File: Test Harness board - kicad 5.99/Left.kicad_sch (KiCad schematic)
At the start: 27 parts

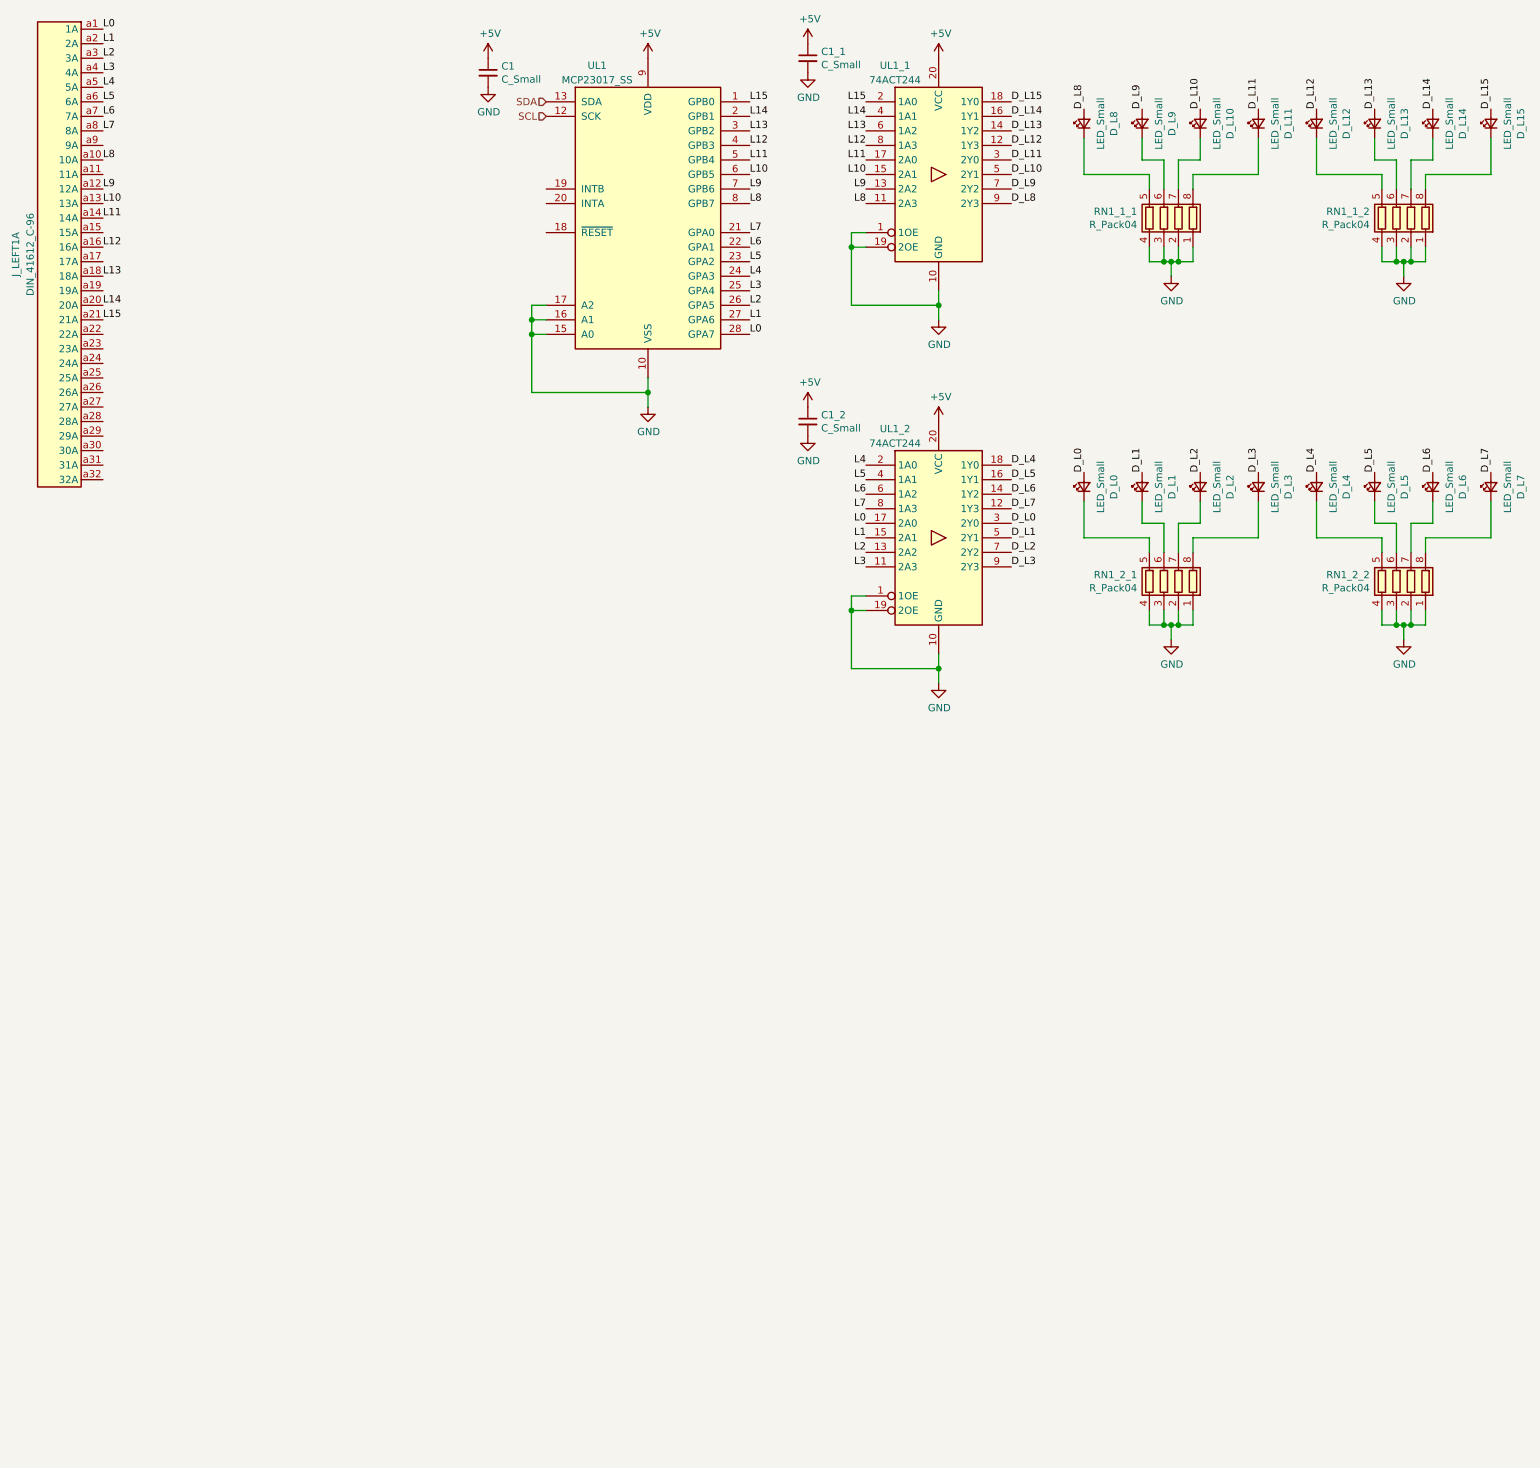
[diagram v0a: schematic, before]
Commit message: add the components to display the MAR bits
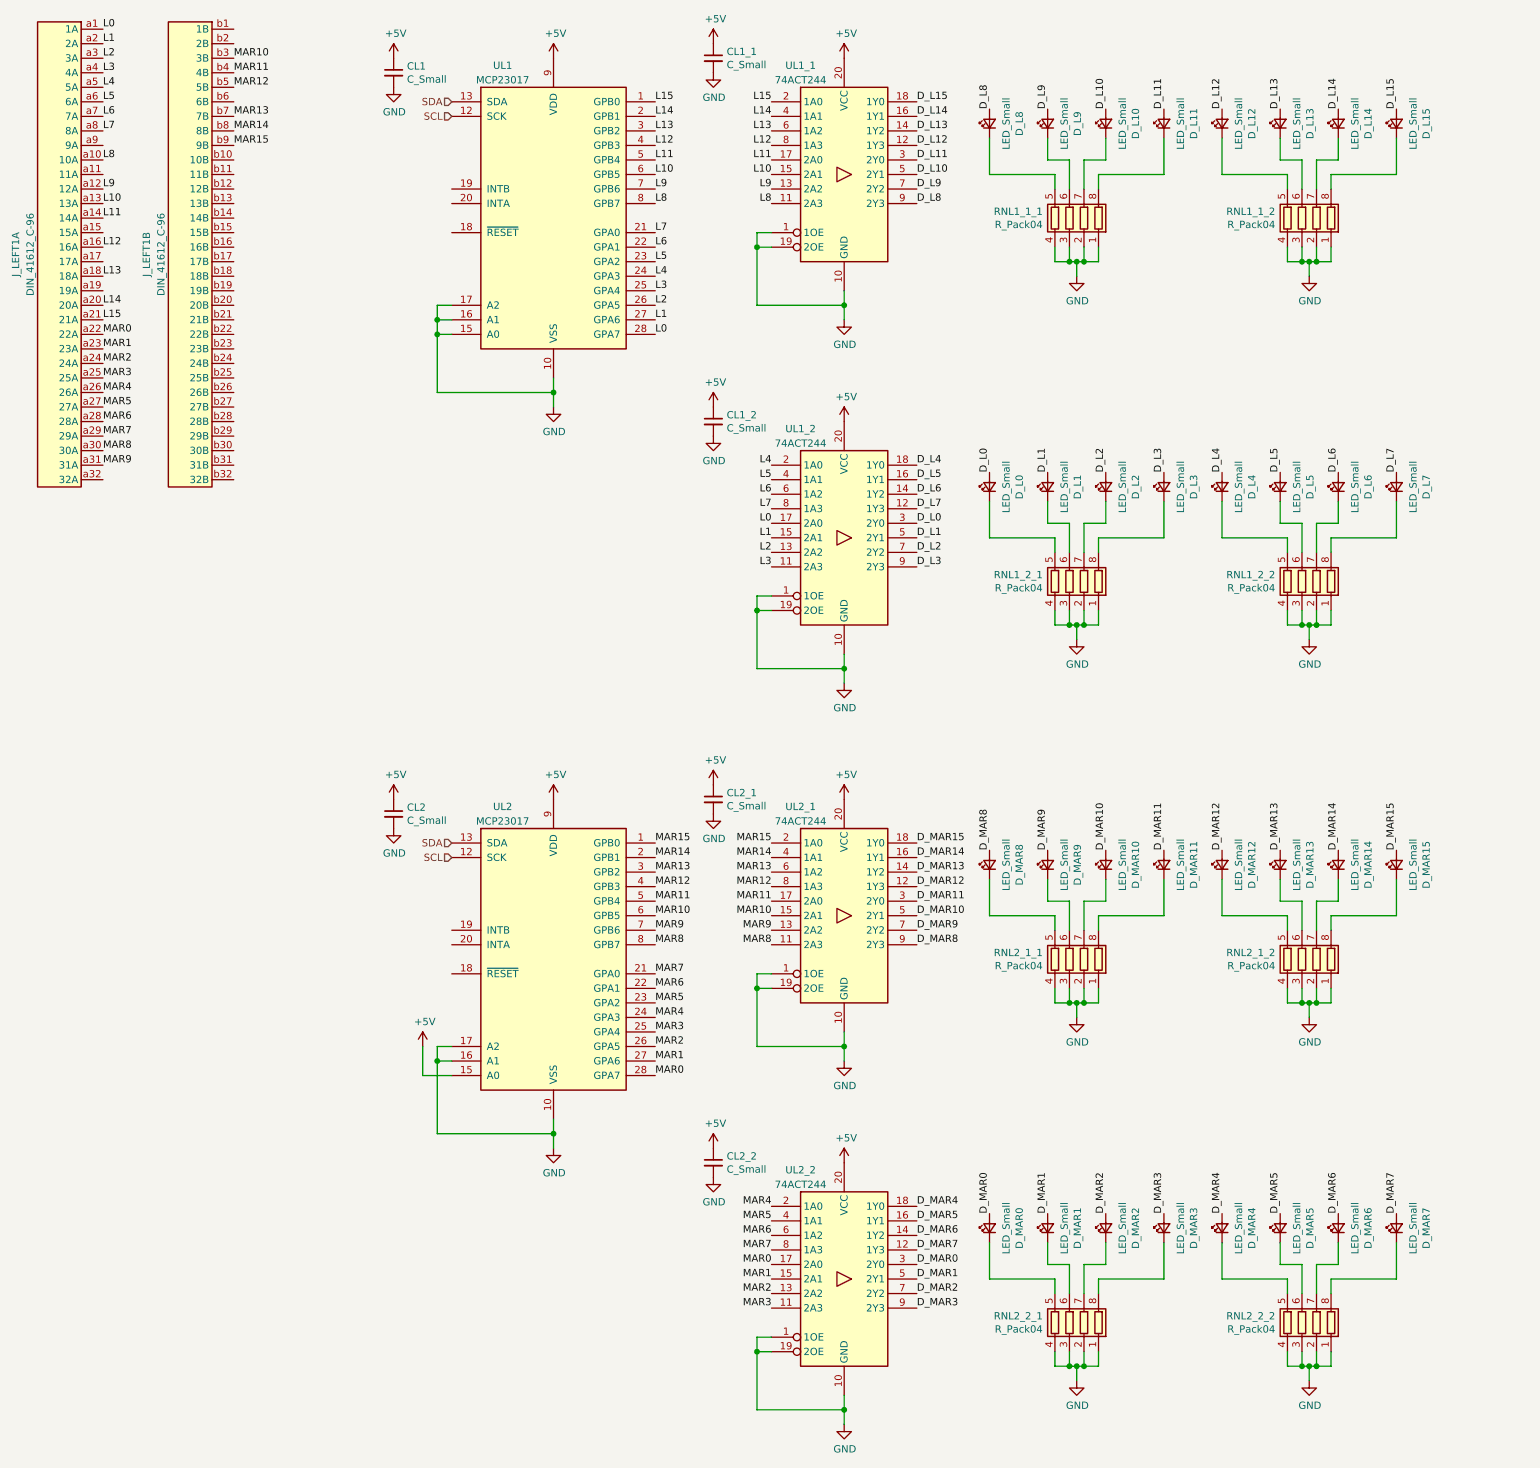
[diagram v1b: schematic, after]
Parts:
- added CL2, CL2_1, CL2_2: C_Small, Capacitor_SMD:C_1206_3216Metric, symbol Device:C_Small
- added D_MAR0, D_MAR1, D_MAR10, D_MAR11, D_MAR12, D_MAR13, D_MAR14, D_MAR15, D_MAR2, D_MAR3, D_MAR4, D_MAR5, D_MAR6, D_MAR7, D_MAR8, D_MAR9: LED_Small, LED_SMD:LED_1206_3216Metric_Castellated, symbol Device:LED_Small
- added unit 2 of J_LEFT1
- added RNL2_1_1, RNL2_1_2, RNL2_2_1, RNL2_2_2: R_Pack04, Resistor_SMD:R_Array_Convex_4x1206, symbol Device:R_Pack04
- added UL2: MCP23017, Package_SO:SSOP-28_5.3x10.2mm_P0.65mm, symbol Interface_Expansion:MCP23017_SS
- added UL2_1, UL2_2: 74ACT244, Package_SO:TSSOP-20_4.4x6.5mm_P0.65mm, symbol 74xx:74HCT244
- UL1: value MCP23017_SS -> MCP23017
- renumbered C1 to CL1, C1_1 to CL1_1, C1_2 to CL1_2, RN1_1_1 to RNL1_1_1, RN1_1_2 to RNL1_1_2, RN1_2_1 to RNL1_2_1, RN1_2_2 to RNL1_2_2
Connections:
- net +5V: now also CL2.1, CL2_1.1, CL2_2.1, UL2.15 (A0), UL2.9 (VDD), UL2_1.20 (VCC), UL2_2.20 (VCC)
- net GND: now also CL2.2, CL2_1.2, CL2_2.2, RNL2_1_1.1 (R1.1), RNL2_1_1.2 (R2.1), RNL2_1_1.3 (R3.1), RNL2_1_1.4 (R4.1), RNL2_1_2.1 (R1.1), RNL2_1_2.2 (R2.1), RNL2_1_2.3 (R3.1), RNL2_1_2.4 (R4.1), RNL2_2_1.1 (R1.1), RNL2_2_1.2 (R2.1), RNL2_2_1.3 (R3.1), RNL2_2_1.4 (R4.1), RNL2_2_2.1 (R1.1), RNL2_2_2.2 (R2.1), RNL2_2_2.3 (R3.1), RNL2_2_2.4 (R4.1), UL2.10 (VSS), UL2.16 (A1), UL2.17 (A2), UL2_1.1 (1OE), UL2_1.10 (GND), UL2_1.19 (2OE), UL2_2.1 (1OE), UL2_2.10 (GND), UL2_2.19 (2OE)
- net SCL: now also UL2.12 (SCK)
- net SDA: now also UL2.13 (SDA)
- net MAR0: now reaches J_LEFT1.a22 (22A)
- net MAR0: now also UL2.28 (GPA7), UL2_2.17 (2A0)
- net MAR1: now reaches J_LEFT1.a23 (23A)
- net MAR1: now also UL2.27 (GPA6), UL2_2.15 (2A1)
- net MAR2: now reaches J_LEFT1.a24 (24A)
- net MAR2: now also UL2.26 (GPA5), UL2_2.13 (2A2)
- net MAR3: now reaches J_LEFT1.a25 (25A)
- net MAR3: now also UL2.25 (GPA4), UL2_2.11 (2A3)
- net MAR4: now reaches J_LEFT1.a26 (26A)
- net MAR4: now also UL2.24 (GPA3), UL2_2.2 (1A0)
- net MAR5: now reaches J_LEFT1.a27 (27A)
- net MAR5: now also UL2.23 (GPA2), UL2_2.4 (1A1)
- net MAR6: now reaches J_LEFT1.a28 (28A)
- net MAR6: now also UL2.22 (GPA1), UL2_2.6 (1A2)
- net MAR7: now reaches J_LEFT1.a29 (29A)
- net MAR7: now also UL2.21 (GPA0), UL2_2.8 (1A3)
- net MAR8: now reaches J_LEFT1.a30 (30A)
- net MAR8: now also UL2.8 (GPB7), UL2_1.11 (2A3)
- net MAR9: now reaches J_LEFT1.a31 (31A)
- net MAR9: now also UL2.7 (GPB6), UL2_1.13 (2A2)
- new net: D_MAR0.1 (K), RNL2_2_1.5 (R4.2)
- new net: D_MAR1.1 (K), RNL2_2_1.6 (R3.2)
- new net: D_MAR15.1 (K), RNL2_1_2.8 (R1.2)
- new net: D_MAR10.1 (K), RNL2_1_1.7 (R2.2)
- new net: D_MAR9.1 (K), RNL2_1_1.6 (R3.2)
- new net: D_MAR11.1 (K), RNL2_1_1.8 (R1.2)
- new net: D_MAR2.1 (K), RNL2_2_1.7 (R2.2)
- new net: D_MAR14.1 (K), RNL2_1_2.7 (R2.2)
- new net: D_MAR8.1 (K), RNL2_1_1.5 (R4.2)
- new net: D_MAR6.1 (K), RNL2_2_2.7 (R2.2)
- new net: D_MAR4.1 (K), RNL2_2_2.5 (R4.2)
- new net: D_MAR3.1 (K), RNL2_2_1.8 (R1.2)
- new net: D_MAR7.1 (K), RNL2_2_2.8 (R1.2)
- new net: D_MAR12.1 (K), RNL2_1_2.5 (R4.2)
- new net: D_MAR13.1 (K), RNL2_1_2.6 (R3.2)
- new net: D_MAR5.1 (K), RNL2_2_2.6 (R3.2)
- new net D_MAR0: D_MAR0.2 (A), UL2_2.3 (2Y0)
- new net D_MAR1: D_MAR1.2 (A), UL2_2.5 (2Y1)
- new net D_MAR10: D_MAR10.2 (A), UL2_1.5 (2Y1)
- new net D_MAR11: D_MAR11.2 (A), UL2_1.3 (2Y0)
- new net D_MAR12: D_MAR12.2 (A), UL2_1.12 (1Y3)
- new net D_MAR13: D_MAR13.2 (A), UL2_1.14 (1Y2)
- new net D_MAR14: D_MAR14.2 (A), UL2_1.16 (1Y1)
- new net D_MAR15: D_MAR15.2 (A), UL2_1.18 (1Y0)
- new net D_MAR2: D_MAR2.2 (A), UL2_2.7 (2Y2)
- new net D_MAR3: D_MAR3.2 (A), UL2_2.9 (2Y3)
- new net D_MAR4: D_MAR4.2 (A), UL2_2.18 (1Y0)
- new net D_MAR5: D_MAR5.2 (A), UL2_2.16 (1Y1)
- new net D_MAR6: D_MAR6.2 (A), UL2_2.14 (1Y2)
- new net D_MAR7: D_MAR7.2 (A), UL2_2.12 (1Y3)
- new net D_MAR8: D_MAR8.2 (A), UL2_1.9 (2Y3)
- new net D_MAR9: D_MAR9.2 (A), UL2_1.7 (2Y2)
- new net MAR10: J_LEFT1.b3 (3B), UL2.6 (GPB5), UL2_1.15 (2A1)
- new net MAR11: J_LEFT1.b4 (4B), UL2.5 (GPB4), UL2_1.17 (2A0)
- new net MAR12: J_LEFT1.b5 (5B), UL2.4 (GPB3), UL2_1.8 (1A3)
- new net MAR13: J_LEFT1.b7 (7B), UL2.3 (GPB2), UL2_1.6 (1A2)
- new net MAR14: J_LEFT1.b8 (8B), UL2.2 (GPB1), UL2_1.4 (1A1)
- new net MAR15: J_LEFT1.b9 (9B), UL2.1 (GPB0), UL2_1.2 (1A0)
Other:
- moved on the sheet: CL1, CL1_1, CL1_2, D_L0, D_L1, D_L10, D_L11, D_L12, D_L13, D_L14, D_L15, D_L2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

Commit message: restart on the test harness, made a more compact design (will need the 4 layers though)
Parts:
- added CL3, CL3_1, CL3_2, CL4, CL4_1, CL4_2, CL5, CL5_1, CL5_2: C_Small, Capacitor_SMD:C_1206_3216Metric, symbol Device:C_Small
- added D_A0, D_A1, D_A10, D_A11, D_A12, D_A13, D_A14, D_A15, D_A16, D_A17, D_A18, D_A19, D_A2, D_A20, D_A21, D_A3, D_A4, D_A5, D_A6, D_A7, D_A8, D_A9, D_D0, D_D1, D_D2, D_D3, D_D4, D_D5, D_D6, D_D7, D_IR2, D_IR3, D_MEMORY1, D_MEMREF1, D_XL_MDR_HI1, D_XL_MDR_LO1, D__IR1, D__IRQ4, D__PSEL1, D__RD1, D__RESET1, D__STOP_CLK1, D__WR1: LED_Small, LED_SMD:LED_1206_3216Metric_Castellated, symbol Device:LED_Small
- added unit 3 of J_LEFT1
- added RNL3_1_1, RNL3_1_2, RNL3_2_1, RNL3_2_2, RNL4_1_1, RNL4_1_2, RNL4_2_1, RNL4_2_2, RNL5_1_1, RNL5_1_2, RNL5_2_1, RNL5_2_2: R_Pack04, Resistor_SMD:R_Array_Convex_4x1206, symbol Device:R_Pack04
- added UL3, UL4, UL5: MCP23017, Package_SO:SSOP-28_5.3x10.2mm_P0.65mm, symbol Interface_Expansion:MCP23017_SS
- added UL3_1, UL3_2, UL4_1, UL4_2, UL5_1, UL5_2: 74ACT244, Package_SO:TSSOP-20_4.4x6.5mm_P0.65mm, symbol 74xx:74HCT244
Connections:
- net +5V: now also CL3.1, CL3_1.1, CL3_2.1, CL4.1, CL4_1.1, CL4_2.1, CL5.1, CL5_1.1, CL5_2.1, UL3.16 (A1), UL3.9 (VDD), UL3_1.20 (VCC), UL3_2.20 (VCC), UL4.15 (A0), UL4.16 (A1), UL4.9 (VDD), UL4_1.20 (VCC), UL4_2.20 (VCC), UL5.15 (A0), UL5.9 (VDD), UL5_1.20 (VCC), UL5_2.20 (VCC)
- net GND: now also CL3.2, CL3_1.2, CL3_2.2, CL4.2, CL4_1.2, CL4_2.2, CL5.2, CL5_1.2, CL5_2.2, RNL3_1_1.1 (R1.1), RNL3_1_1.2 (R2.1), RNL3_1_1.3 (R3.1), RNL3_1_1.4 (R4.1), RNL3_1_2.1 (R1.1), RNL3_1_2.2 (R2.1), RNL3_1_2.3 (R3.1), RNL3_1_2.4 (R4.1), RNL3_2_1.1 (R1.1), RNL3_2_1.2 (R2.1), RNL3_2_1.3 (R3.1), RNL3_2_1.4 (R4.1), RNL3_2_2.1 (R1.1), RNL3_2_2.2 (R2.1), RNL3_2_2.3 (R3.1), RNL3_2_2.4 (R4.1), RNL4_1_1.1 (R1.1), RNL4_1_1.2 (R2.1), RNL4_1_1.3 (R3.1), RNL4_1_1.4 (R4.1), RNL4_1_2.1 (R1.1), RNL4_1_2.2 (R2.1), RNL4_1_2.3 (R3.1), RNL4_1_2.4 (R4.1), RNL4_2_1.1 (R1.1), RNL4_2_1.2 (R2.1), RNL4_2_1.3 (R3.1), RNL4_2_1.4 (R4.1), RNL4_2_2.1 (R1.1), RNL4_2_2.2 (R2.1), RNL4_2_2.3 (R3.1), RNL4_2_2.4 (R4.1), RNL5_1_1.1 (R1.1), RNL5_1_1.2 (R2.1), RNL5_1_1.3 (R3.1), RNL5_1_1.4 (R4.1), RNL5_1_2.1 (R1.1), RNL5_1_2.2 (R2.1), RNL5_1_2.3 (R3.1), RNL5_1_2.4 (R4.1), RNL5_2_1.1 (R1.1), RNL5_2_1.2 (R2.1), RNL5_2_1.3 (R3.1), RNL5_2_1.4 (R4.1), RNL5_2_2.1 (R1.1), RNL5_2_2.2 (R2.1), RNL5_2_2.3 (R3.1), RNL5_2_2.4 (R4.1), UL3.10 (VSS), UL3.15 (A0), UL3.17 (A2), UL3_1.1 (1OE), UL3_1.10 (GND), UL3_1.19 (2OE), UL3_2.1 (1OE), UL3_2.10 (GND), UL3_2.19 (2OE), UL4.10 (VSS), UL4.17 (A2), UL4_1.1 (1OE), UL4_1.10 (GND), UL4_1.11 (2A3), UL4_1.13 (2A2), UL4_1.19 (2OE), UL4_2.1 (1OE), UL4_2.10 (GND), UL4_2.19 (2OE), UL5.10 (VSS), UL5.16 (A1), UL5.17 (A2), UL5_1.1 (1OE), UL5_1.10 (GND), UL5_1.19 (2OE), UL5_2.1 (1OE), UL5_2.10 (GND), UL5_2.19 (2OE)
- net SCL: now also UL3.12 (SCK), UL4.12 (SCK), UL5.12 (SCK)
- net SDA: now also UL3.13 (SDA), UL4.13 (SDA), UL5.13 (SDA)
- net MEMREF: now reaches J_LEFT1.b10 (10B)
- net MEMREF: now also UL5.3 (GPB2), UL5_1.6 (1A2)
- net _RESET: now reaches J_LEFT1.b14 (14B)
- net _RESET: now also UL5.4 (GPB3), UL5_1.8 (1A3)
- net _STOP_CLK: now reaches J_LEFT1.b15 (15B)
- net _STOP_CLK: now also UL5.5 (GPB4), UL5_1.17 (2A0)
- net _WR: now reaches J_LEFT1.b16 (16B)
- net _WR: now also UL5.23 (GPA2), UL5_2.6 (1A2)
- net XL_MDR_HI: now reaches J_LEFT1.b18 (18B)
- net XL_MDR_HI: now also UL5.25 (GPA4), UL5_2.17 (2A0)
- net XL_MDR_LO: now reaches J_LEFT1.b19 (19B)
- net XL_MDR_LO: now also UL5.24 (GPA3), UL5_2.8 (1A3)
- net MEMORY: now reaches J_LEFT1.b2 (2B)
- net MEMORY: now also UL5.1 (GPB0), UL5_1.2 (1A0)
- net _RD: now reaches J_LEFT1.b25 (25B)
- net _RD: now also UL5.22 (GPA1), UL5_2.4 (1A1)
- net _IRQ4: now reaches J_LEFT1.b26 (26B)
- net _IRQ4: now also UL5.8 (GPB7), UL5_1.11 (2A3)
- net IR1: now reaches J_LEFT1.b28 (28B)
- net IR1: now also UL5.28 (GPA7), UL5_2.11 (2A3)
- net IR2: now reaches J_LEFT1.b29 (29B)
- net IR2: now also UL5.27 (GPA6), UL5_2.13 (2A2)
- net IR3: now reaches J_LEFT1.b30 (30B)
- net IR3: now also UL5.26 (GPA5), UL5_2.15 (2A1)
- net _PSEL1: now reaches J_LEFT1.b6 (6B)
- net _PSEL1: now also UL5.21 (GPA0), UL5_2.2 (1A0)
- new net: D__RD1.1 (K), RNL5_2_1.7 (R2.2)
- new net: D_A16.1 (K), RNL3_1_1.7 (R2.2)
- new net: D_D6.1 (K), RNL4_2_2.7 (R2.2)
- new net: D_A14.1 (K), RNL3_1_1.5 (R4.2)
- new net: D_A6.1 (K), RNL3_2_1.5 (R4.2)
- new net: D_A7.1 (K), RNL3_2_1.6 (R3.2)
- new net: D_A8.1 (K), RNL3_2_1.7 (R2.2)
- new net: D_A9.1 (K), RNL3_2_1.8 (R1.2)
- new net: D_A15.1 (K), RNL3_1_1.6 (R3.2)
- new net: D_A17.1 (K), RNL3_1_1.8 (R1.2)
- new net: D_A0.1 (K), RNL4_1_1.7 (R2.2)
- new net: D_XL_MDR_LO1.1 (K), RNL5_2_1.5 (R4.2)
- new net: D_A20.1 (K), RNL3_1_2.7 (R2.2)
- new net: D__WR1.1 (K), RNL5_2_1.6 (R3.2)
- new net: D__PSEL1.1 (K), RNL5_2_1.8 (R1.2)
- new net: D__IR1.1 (K), RNL5_2_2.5 (R4.2)
- new net: D_IR2.1 (K), RNL5_2_2.6 (R3.2)
- new net: D_IR3.1 (K), RNL5_2_2.7 (R2.2)
- new net: D_XL_MDR_HI1.1 (K), RNL5_2_2.8 (R1.2)
- new net: D_D3.1 (K), RNL4_2_1.8 (R1.2)
- new net: D_A11.1 (K), RNL3_2_2.6 (R3.2)
- new net: D_A1.1 (K), RNL4_1_1.8 (R1.2)
- new net: D_A19.1 (K), RNL3_1_2.6 (R3.2)
- new net: D_MEMREF1.1 (K), RNL5_1_1.5 (R4.2)
- new net: D_MEMORY1.1 (K), RNL5_1_1.6 (R3.2)
- new net: D__RESET1.1 (K), RNL5_1_1.7 (R2.2)
- new net: D__STOP_CLK1.1 (K), RNL5_1_1.8 (R1.2)
- new net: D_D7.1 (K), RNL4_2_2.8 (R1.2)
- new net: D_D1.1 (K), RNL4_2_1.6 (R3.2)
- new net: D__IRQ4.1 (K), RNL5_1_2.7 (R2.2)
- new net: D_A5.1 (K), RNL4_1_2.8 (R1.2)
- new net: D_D5.1 (K), RNL4_2_2.6 (R3.2)
- new net: D_D4.1 (K), RNL4_2_2.5 (R4.2)
- new net: D_A21.1 (K), RNL3_1_2.8 (R1.2)
- new net: D_D2.1 (K), RNL4_2_1.7 (R2.2)
- new net: D_D0.1 (K), RNL4_2_1.5 (R4.2)
- new net: D_A4.1 (K), RNL4_1_2.7 (R2.2)
- new net: D_A12.1 (K), RNL3_2_2.7 (R2.2)
- new net: D_A2.1 (K), RNL4_1_2.5 (R4.2)
- new net: D_A3.1 (K), RNL4_1_2.6 (R3.2)
- new net: D_A10.1 (K), RNL3_2_2.5 (R4.2)
- new net: D_A18.1 (K), RNL3_1_2.5 (R4.2)
- new net: D_A13.1 (K), RNL3_2_2.8 (R1.2)
- new net A0: J_LEFT1.c1 (1C), UL4.6 (GPB5), UL4_1.15 (2A1)
- new net A1: J_LEFT1.c2 (2C), UL4.5 (GPB4), UL4_1.17 (2A0)
- new net A10: J_LEFT1.c12 (12C), UL3.24 (GPA3), UL3_2.8 (1A3)
- new net A11: J_LEFT1.c13 (13C), UL3.23 (GPA2), UL3_2.6 (1A2)
- new net A12: J_LEFT1.c14 (14C), UL3.22 (GPA1), UL3_2.4 (1A1)
- new net A13: J_LEFT1.c15 (15C), UL3.21 (GPA0), UL3_2.2 (1A0)
- new net A14: J_LEFT1.c16 (16C), UL3.8 (GPB7), UL3_1.11 (2A3)
- new net A15: J_LEFT1.c17 (17C), UL3.7 (GPB6), UL3_1.13 (2A2)
- new net A16: J_LEFT1.c18 (18C), UL3.6 (GPB5), UL3_1.15 (2A1)
- new net A17: J_LEFT1.c19 (19C), UL3.5 (GPB4), UL3_1.17 (2A0)
- new net A18: J_LEFT1.c20 (20C), UL3.4 (GPB3), UL3_1.8 (1A3)
- new net A19: J_LEFT1.c21 (21C), UL3.3 (GPB2), UL3_1.6 (1A2)
- new net A2: J_LEFT1.c3 (3C), UL4.4 (GPB3), UL4_1.8 (1A3)
- new net A20: J_LEFT1.c22 (22C), UL3.2 (GPB1), UL3_1.4 (1A1)
- new net A21: J_LEFT1.c23 (23C), UL3.1 (GPB0), UL3_1.2 (1A0)
- new net A3: J_LEFT1.c4 (4C), UL4.3 (GPB2), UL4_1.6 (1A2)
- new net A4: J_LEFT1.c5 (5C), UL4.2 (GPB1), UL4_1.4 (1A1)
- new net A5: J_LEFT1.c6 (6C), UL4.1 (GPB0), UL4_1.2 (1A0)
- new net A6: J_LEFT1.c7 (7C), UL3.28 (GPA7), UL3_2.11 (2A3)
- new net A7: J_LEFT1.c8 (8C), UL3.27 (GPA6), UL3_2.13 (2A2)
- new net A8: J_LEFT1.c10 (10C), UL3.26 (GPA5), UL3_2.15 (2A1)
- new net A9: J_LEFT1.c11 (11C), UL3.25 (GPA4), UL3_2.17 (2A0)
- new net D0: J_LEFT1.c24 (24C), UL4.28 (GPA7), UL4_2.17 (2A0)
- new net D1: J_LEFT1.c25 (25C), UL4.27 (GPA6), UL4_2.15 (2A1)
- new net D2: J_LEFT1.c26 (26C), UL4.26 (GPA5), UL4_2.13 (2A2)
- new net D3: J_LEFT1.c27 (27C), UL4.25 (GPA4), UL4_2.11 (2A3)
- new net D4: J_LEFT1.c28 (28C), UL4.24 (GPA3), UL4_2.2 (1A0)
- new net D5: J_LEFT1.c29 (29C), UL4.23 (GPA2), UL4_2.4 (1A1)
- new net D6: J_LEFT1.c30 (30C), UL4.22 (GPA1), UL4_2.6 (1A2)
- new net D7: J_LEFT1.c31 (31C), UL4.21 (GPA0), UL4_2.8 (1A3)
- new net D_A0: D_A0.2 (A), UL4_1.5 (2Y1)
- new net D_A1: D_A1.2 (A), UL4_1.3 (2Y0)
- new net D_A10: D_A10.2 (A), UL3_2.12 (1Y3)
- new net D_A11: D_A11.2 (A), UL3_2.14 (1Y2)
- new net D_A12: D_A12.2 (A), UL3_2.16 (1Y1)
- new net D_A13: D_A13.2 (A), UL3_2.18 (1Y0)
- new net D_A14: D_A14.2 (A), UL3_1.9 (2Y3)
- new net D_A15: D_A15.2 (A), UL3_1.7 (2Y2)
- new net D_A16: D_A16.2 (A), UL3_1.5 (2Y1)
- new net D_A17: D_A17.2 (A), UL3_1.3 (2Y0)
- new net D_A18: D_A18.2 (A), UL3_1.12 (1Y3)
- new net D_A19: D_A19.2 (A), UL3_1.14 (1Y2)
- new net D_A2: D_A2.2 (A), UL4_1.12 (1Y3)
- new net D_A20: D_A20.2 (A), UL3_1.16 (1Y1)
- new net D_A21: D_A21.2 (A), UL3_1.18 (1Y0)
- new net D_A3: D_A3.2 (A), UL4_1.14 (1Y2)
- new net D_A4: D_A4.2 (A), UL4_1.16 (1Y1)
- new net D_A5: D_A5.2 (A), UL4_1.18 (1Y0)
- new net D_A6: D_A6.2 (A), UL3_2.9 (2Y3)
- new net D_A7: D_A7.2 (A), UL3_2.7 (2Y2)
- new net D_A8: D_A8.2 (A), UL3_2.5 (2Y1)
- new net D_A9: D_A9.2 (A), UL3_2.3 (2Y0)
- new net D_D0: D_D0.2 (A), UL4_2.3 (2Y0)
- new net D_D1: D_D1.2 (A), UL4_2.5 (2Y1)
- new net D_D2: D_D2.2 (A), UL4_2.7 (2Y2)
- new net D_D3: D_D3.2 (A), UL4_2.9 (2Y3)
- new net D_D4: D_D4.2 (A), UL4_2.18 (1Y0)
- new net D_D5: D_D5.2 (A), UL4_2.16 (1Y1)
- new net D_D6: D_D6.2 (A), UL4_2.14 (1Y2)
- new net D_D7: D_D7.2 (A), UL4_2.12 (1Y3)
- new net D_IR1: D__IR1.2 (A), UL5_2.9 (2Y3)
- new net D_IR2: D_IR2.2 (A), UL5_2.7 (2Y2)
- new net D_IR3: D_IR3.2 (A), UL5_2.5 (2Y1)
- new net D_MEMORY: D_MEMORY1.2 (A), UL5_1.18 (1Y0)
- new net D_MEMREF: D_MEMREF1.2 (A), UL5_1.14 (1Y2)
- new net D_WR: UL5_2.14 (1Y2)
- new net D_XL_MDR_HI: D_XL_MDR_HI1.2 (A), UL5_2.3 (2Y0)
- new net D_XL_MDR_LO: D_XL_MDR_LO1.2 (A), UL5_2.12 (1Y3)
- new net D__IRQ4: D__IRQ4.2 (A), UL5_1.9 (2Y3)
- new net D__PSEL1: D__PSEL1.2 (A), UL5_2.18 (1Y0)
- new net D__RD: D__RD1.2 (A), UL5_2.16 (1Y1)
- new net D__RESET: D__RESET1.2 (A), UL5_1.12 (1Y3)
- new net D__STOP_CLK: D__STOP_CLK1.2 (A), UL5_1.3 (2Y0)
- new net D__WR: D__WR1.2 (A)
- no-connect marks 0 -> 4
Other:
- moved on the sheet: CL1, CL1_1, CL1_2, CL2, CL2_1, CL2_2, D_L0, D_L1, D_L10, D_L11, D_L12, D_L13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

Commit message: restart with the test harness board
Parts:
- J_LEFT1: footprint (none) -> Connector_DIN:DIN41612_C_3x32_Male_Horizontal_THT
- UL1, UL2, UL3, UL4, UL5: footprint Package_SO:SSOP-28_5.3x10.2mm_P0.65mm -> Package_SO:SOIC-28W_7.5x17.9mm_P1.27mm
- UL1_1, UL1_2, UL2_1, UL2_2, UL3_1, UL3_2, UL4_1, UL4_2, UL5_1, UL5_2: footprint Package_SO:TSSOP-20_4.4x6.5mm_P0.65mm -> Package_SO:SOIC-20W_7.5x12.8mm_P1.27mm
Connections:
- net D_WR is gone; now on net D__WR: UL5_2.14 (1Y2)
- net +5V: now also J_LEFT1.a32 (32A), J_LEFT1.b1 (1B), J_LEFT1.b11 (11B), J_LEFT1.b13 (13B), J_LEFT1.b17 (17B), J_LEFT1.b21 (21B), J_LEFT1.b24 (24B), J_LEFT1.b27 (27B), J_LEFT1.b32 (32B), J_LEFT1.c32 (32C)
- net A10: now also UL3.4 (GPB3); no longer UL3.24 (GPA3)
- net A11: now also UL3.3 (GPB2); no longer UL3.23 (GPA2)
- net A12: now also UL3.2 (GPB1); no longer UL3.22 (GPA1)
- net A13: now also UL3.1 (GPB0); no longer UL3.21 (GPA0)
- net A14: now also UL3.28 (GPA7); no longer UL3.8 (GPB7)
- net A15: now also UL3.27 (GPA6); no longer UL3.7 (GPB6)
- net A16: now also UL3.26 (GPA5); no longer UL3.6 (GPB5)
- net A17: now also UL3.25 (GPA4); no longer UL3.5 (GPB4)
- net A18: now also UL3.24 (GPA3); no longer UL3.4 (GPB3)
- net A19: now also UL3.23 (GPA2); no longer UL3.3 (GPB2)
- net A20: now also UL3.22 (GPA1); no longer UL3.2 (GPB1)
- net A21: now also UL3.21 (GPA0); no longer UL3.1 (GPB0)
- net A6: now also UL3.8 (GPB7); no longer UL3.28 (GPA7)
- net A7: now also UL3.7 (GPB6); no longer UL3.27 (GPA6)
- net A8: now also UL3.6 (GPB5); no longer UL3.26 (GPA5)
- net A9: now also UL3.5 (GPB4); no longer UL3.25 (GPA4)
- net D_MEMORY: now also UL5_1.5 (2Y1); no longer UL5_1.18 (1Y0)
- net D_MEMREF: now also UL5_1.3 (2Y0); no longer UL5_1.14 (1Y2)
- net D__IRQ4: now also UL5_1.12 (1Y3); no longer UL5_1.9 (2Y3)
- net D__RESET: now also UL5_1.7 (2Y2); no longer UL5_1.12 (1Y3)
- net D__STOP_CLK: now also UL5_1.9 (2Y3); no longer UL5_1.3 (2Y0)
- net GND: now also J_LEFT1.a11 (11A), J_LEFT1.a15 (15A), J_LEFT1.a17 (17A), J_LEFT1.a19 (19A), J_LEFT1.a9 (9A), J_LEFT1.b12 (12B), J_LEFT1.b20 (20B), J_LEFT1.b22 (22B), J_LEFT1.b23 (23B), J_LEFT1.b31 (31B), J_LEFT1.c9 (9C)
- net IR1: now also UL5.21 (GPA0); no longer UL5.28 (GPA7)
- net IR2: now also UL5.22 (GPA1); no longer UL5.27 (GPA6)
- net IR3: now also UL5.23 (GPA2); no longer UL5.26 (GPA5)
- net MEMORY: now also UL5.6 (GPB5), UL5_1.15 (2A1); no longer UL5.1 (GPB0), UL5_1.2 (1A0)
- net MEMREF: now also UL5.5 (GPB4), UL5_1.17 (2A0); no longer UL5.3 (GPB2), UL5_1.6 (1A2)
- net XL_MDR_HI: now also UL5.24 (GPA3); no longer UL5.25 (GPA4)
- net XL_MDR_LO: now also UL5.25 (GPA4); no longer UL5.24 (GPA3)
- net _IRQ4: now also UL5.4 (GPB3), UL5_1.8 (1A3); no longer UL5.8 (GPB7), UL5_1.11 (2A3)
- net _PSEL1: now also UL5.28 (GPA7); no longer UL5.21 (GPA0)
- net _RD: now also UL5.27 (GPA6); no longer UL5.22 (GPA1)
- net _RESET: now also UL5.7 (GPB6), UL5_1.13 (2A2); no longer UL5.4 (GPB3), UL5_1.8 (1A3)
- net _STOP_CLK: now also UL5.8 (GPB7), UL5_1.11 (2A3); no longer UL5.5 (GPB4), UL5_1.17 (2A0)
- net _WR: now also UL5.26 (GPA5); no longer UL5.23 (GPA2)
